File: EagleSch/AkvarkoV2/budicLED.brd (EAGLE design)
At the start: 114.3 x 160 mm, 72 parts, among them IC1 7805T, IC2 4051N, IC3 LF33CV, IC4 ESP01, Q1 BD243C, Q2 BD243C, Q3 BD243C, Q4 BD243C, T1 2N5551, T2 2N5551, T3 2N5551, T4 2N5551, U1 ARDUINOR3-DIMENSION, X1 SMKDSP_1,5/2, X2 SMKDSP_1,5/8, X3 SMKDSP_1,5/3

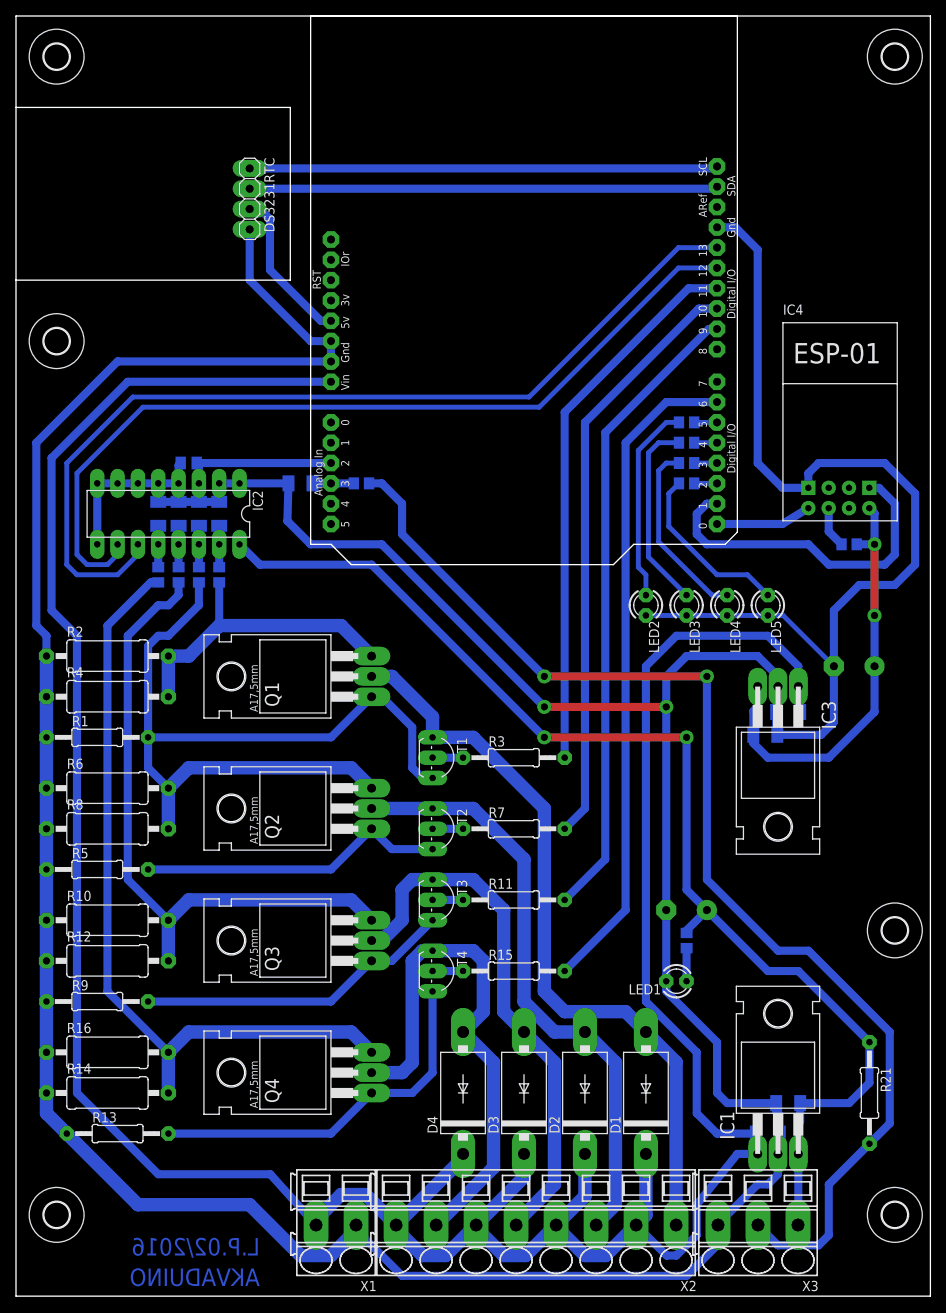
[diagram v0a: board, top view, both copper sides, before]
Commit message: Pridan slot pro SD kartu, odstraneny signalizacni diody.
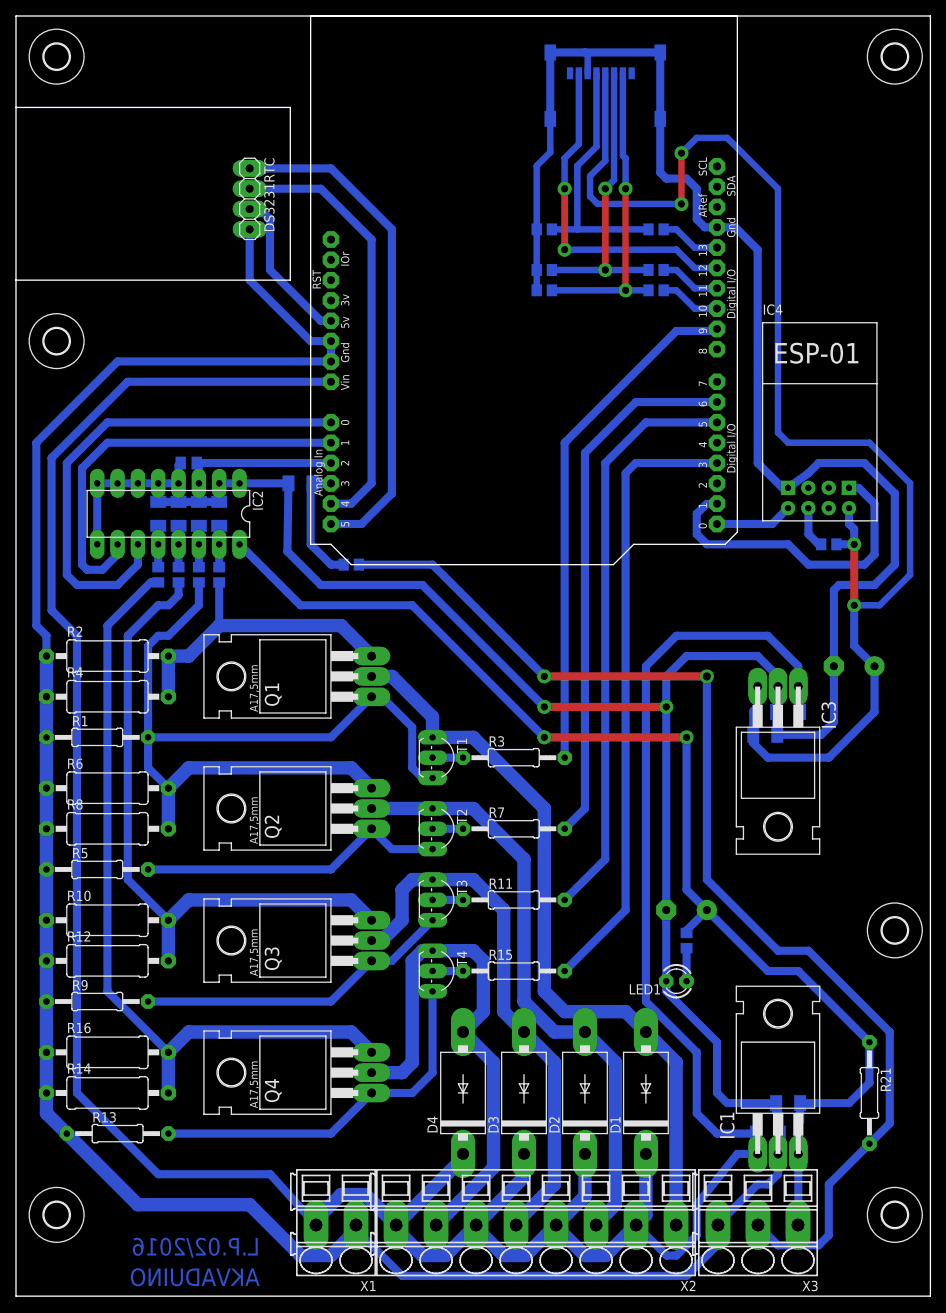
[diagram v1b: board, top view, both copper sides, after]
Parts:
- removed LED2, LED3, LED4, LED5: 2.2V 5mA, led:LED3MM
- added J1: TRANSFLASH-LOCK, sd-mmc:TRANSFLASH-LOCK-SOCK
- added R29: 1k8, rcl:R0805
- added R30: 3k3, rcl:R0805
- R25, R27: value 4k7 -> 1k8
- R26, R28: value 4k7 -> 3k3
- moved R28 32.1 mm to (66.0, 128.3), turned to 0 degrees
- moved R26 32.1 mm to (66.0, 133.3), turned to 0 degrees
- moved R27 24.4 mm to (80.0, 128.3), turned to 0 degrees
- moved R25 24.4 mm to (80.0, 133.3), turned to 0 degrees
- moved R24 10.2 mm to (41.9, 91.4)
- moved IC4 2.54 mm to (100.3, 106.7)
- moved R23 2.54 mm to (101.6, 94.0)
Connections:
- removed net N$20: IC2.11, U1.D13
- removed net N$38: LED5.A, R28.1
- removed net N$39: LED4.A, R27.1
- removed net N$40: LED3.A, R26.1
- removed net N$41: LED2.A, R25.1
- new net MISO: J1.7, U1.D12
- new net MOSI: R27.1, U1.D11
- new net SCK: R25.1, U1.D13
- new net SS: R29.1, U1.D10
- net +3V3: now also J1.4
- net GND: now also J1.6, J1.S1, J1.S2, J1.S3, J1.S4, R26.2, R28.2, R30.2; no longer LED2.K, LED3.K, LED4.K, LED5.K
- net N$13: now also U1.A5; no longer U1.SCL
- net N$15: now also U1.D5; no longer U1.D9
- net N$16: now also R3.2, U1.D9; no longer R28.2, U1.D2
- net N$22: now also U1.D6; no longer U1.D10
- net N$24: now also U1.A4; no longer U1.SDA
- net N$26: now also IC2.11, U1.A0; no longer R27.2, U1.D3
- net N$28: no longer U1.D1
- net N$32: now also J1.5, R25.2, R26.1; no longer IC2.10, U1.D12
- net N$34: now also IC2.10, U1.A1; no longer R3.2, U1.D11
- net N$35: now also U1.D3; no longer U1.D6
- net N$36: now also J1.3, R27.2, R28.1; no longer R26.2, U1.D4
- net N$37: now also J1.2, R29.2, R30.1; no longer R25.2, U1.D5
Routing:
- net +3V3: track 53.5 -> 174.0 mm, vias 2 -> 4
- net N$20: track 116.9 -> 0.00 mm
- net N$32: track 108.2 -> 32.6 mm
- net N$16: track 2.86 -> 64.3 mm
- net N$26: track 2.86 -> 62.1 mm
- net GND: track 582.9 -> 628.3 mm
- net MISO: track 0.00 -> 42.8 mm, vias 0 -> 2
- net N$37: track 2.86 -> 39.3 mm, vias 0 -> 2
- net N$36: track 2.86 -> 37.1 mm, vias 0 -> 2
- net N$41: track 25.0 -> 0.00 mm
- net N$40: track 24.1 -> 0.00 mm
- net N$39: track 23.2 -> 0.00 mm
- net N$38: track 21.9 -> 0.00 mm
- net N$34: track 68.6 -> 51.3 mm
- net N$21: track 5.17 -> 15.2 mm
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
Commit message: Na DPS: - upraveno napajeni - zmenena pouzdra rezistoru u SD karty - seriova linka vyvedena na kolikovou listu - zvetsena sirka spoje GND, doplnen jeden filtracni kapacitor k SD slotu
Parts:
- added C13: 100n, rcl:C1206K
- added JP1: (no value), pinhead:2X04
- added R31: 1k8, rcl:0207/12
- added R32: 3k3, rcl:0207/12
- R25, R26, R27, R28, R29, R30: device rcl:R0805 -> rcl:0207/12
- moved R23 22.9 mm to (101.6, 116.8)
- moved IC4 21.6 mm to (100.3, 128.3)
- moved R21 13.3 mm to (102.9, 12.7)
- moved IC3 12.6 mm to (104.1, 72.4), turned to 270 degrees
- moved C10 11.6 mm to (102.9, 90.2), turned to 180 degrees
- moved R29 8.98 mm to (71.1, 124.5), turned to 90 degrees
- moved R26 8.13 mm to (59.7, 128.3)
- moved R25 8.03 mm to (72.4, 135.9)
- moved R30 7.73 mm to (64.8, 133.3)
- moved J1 7.73 mm to (66.0, 153.7)
- moved R27 6.48 mm to (73.7, 127.0), turned to 90 degrees
- moved R28 4.58 mm to (62.2, 130.8)
- moved C8 3.86 mm to (97.5, 70.8), turned to 90 degrees
- moved C9 2.01 mm to (94.6, 73.7), turned to 270 degrees
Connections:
- new net N$20: IC4.TX, JP1.2, JP1.8
- new net N$38: JP1.5, U1.D1
- new net N$39: IC4.RX, R31.2, R32.1
- new net N$41: JP1.7, U1.D0
- new net N$42: JP1.1, U1.D8
- net +3V3: now also C13.1
- net GND: now also C13.2, R32.2
- net N$25: now also JP1.4, JP1.6, R31.1; no longer IC4.TX, U1.D0
- net N$28: now also JP1.3, U1.D7; no longer IC4.RX
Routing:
- net N$20: track 0.00 -> 32.6 mm
- net N$28: track 39.0 -> 17.6 mm
- net N$39: track 0.00 -> 19.4 mm
- net GND: track 628.3 -> 647.2 mm
- net N$42: track 0.00 -> 16.9 mm
- net N$37: track 39.3 -> 24.5 mm, vias 2 -> 0
- net +3V3: track 174.0 -> 161.7 mm
- net SS: track 7.62 -> 18.7 mm
- net MISO: track 42.8 -> 53.3 mm, vias 2 -> 0
- net MOSI: track 7.62 -> 16.2 mm
- net N$41: track 0.00 -> 6.35 mm
- net N$38: track 0.00 -> 6.35 mm
- net N$32: track 32.6 -> 26.3 mm
- net N$25: track 9.70 -> 6.35 mm
- net SCK: track 7.62 -> 10.9 mm
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
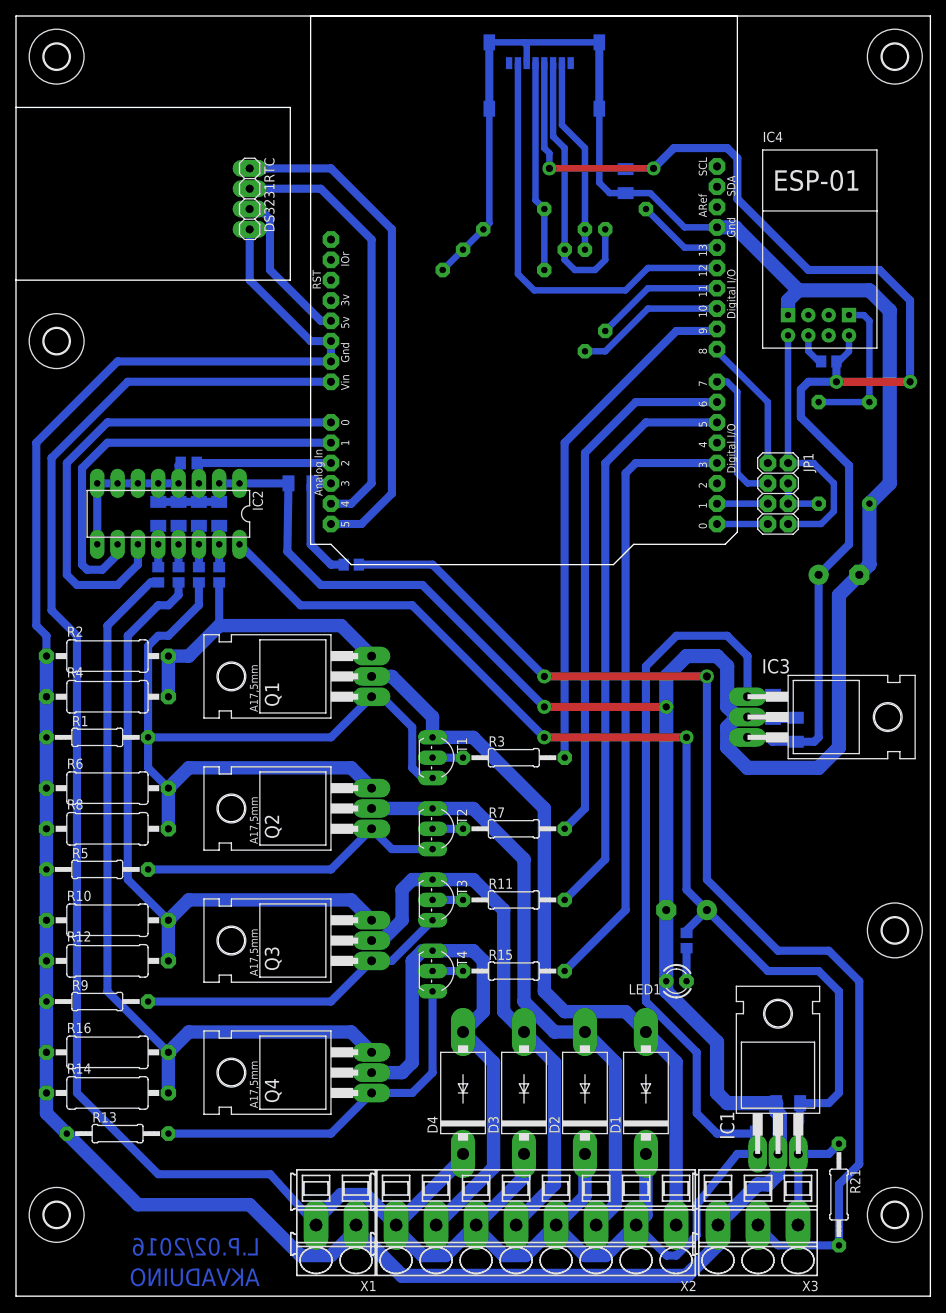
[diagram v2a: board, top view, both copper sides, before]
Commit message: DPS pred vyrobou, nutna kontrola rozmeru.
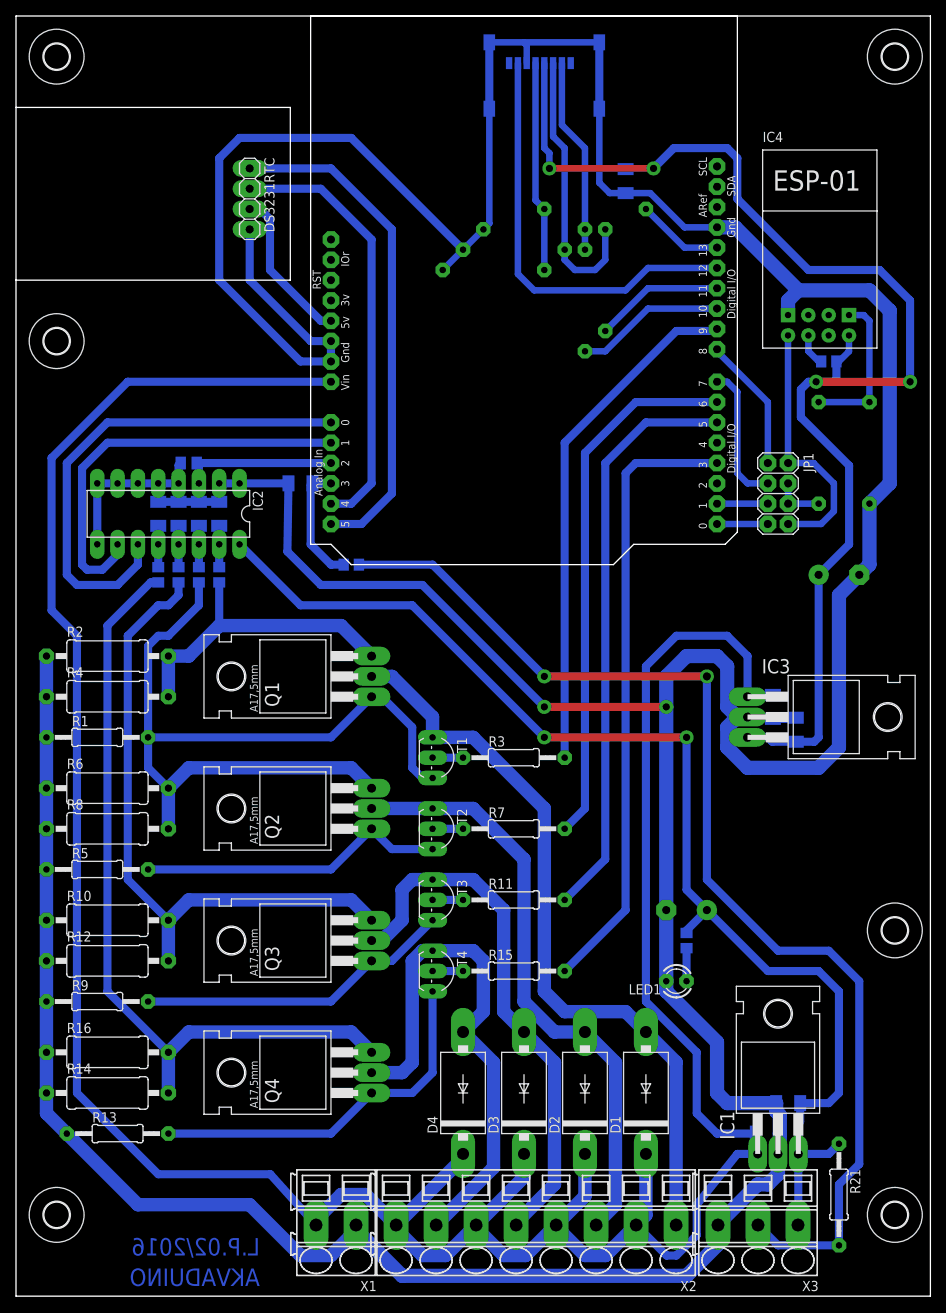
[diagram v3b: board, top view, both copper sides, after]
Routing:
- net +3V3: track 161.7 -> 164.2 mm
- net GND: track 647.2 -> 649.7 mm
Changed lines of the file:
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@@
 <wire x1="34.29" y1="148.59" x2="34.29" y2="127" width="0" layer="20"/>
 <wire x1="34.29" y1="127" x2="0" y2="127" width="0" layer="20"/>
+<dimension x1="0" y1="0" x2="114.3" y2="0" x3="57.15" y3="-8.89" textsize="1.778" layer="48"/>
+<dimension x1="114.3" y1="0" x2="114.3" y2="160.02" x3="124.46" y3="80.01" textsize="1.778" layer="48"/>
+<dimension x1="0" y1="148.59" x2="34.29" y2="148.59" x3="17.145" y3="149.86" textsize="1.778" layer="48"/>
+<dimension x1="0" y1="127" x2="0" y2="148.59" x3="15.24" y3="137.795" textsize="1.778" layer="48"/>
 </plain>
 <attributes>
@@
 <contactref element="U1" pad="GND1"/>
 <wire x1="39.37" y1="116.84" x2="39.37" y2="119.38" width="1.016" layer="16"/>
-<wire x1="12.7" y1="116.84" x2="2.54" y2="106.68" width="1.016" layer="16"/>
 <wire x1="87.75" y1="9.01" x2="92.71" y2="13.97" width="1.778" layer="16"/>
 <wire x1="92.71" y1="13.97" x2="93.98" y2="13.97" width="1.778" layer="16"/>
@@
 <wire x1="42.505" y1="8.295" x2="42.505" y2="8.215" width="1.6764" layer="16"/>
 <wire x1="42.505" y1="8.215" x2="39.37" y2="5.08" width="1.6764" layer="16"/>
-<wire x1="3.81" y1="80.01" x2="3.81" y2="82.55" width="1.016" layer="16"/>
-<wire x1="3.81" y1="82.55" x2="2.54" y2="83.82" width="1.016" layer="16"/>
-<wire x1="2.54" y1="83.82" x2="2.54" y2="106.68" width="1.016" layer="16"/>
-<wire x1="12.7" y1="116.84" x2="39.37" y2="116.84" width="1.016" layer="16"/>
 <wire x1="39.37" y1="119.38" x2="36.83" y2="119.38" width="1.016" layer="16"/>
 <wire x1="36.83" y1="119.38" x2="29.21" y2="127" width="1.016" layer="16"/>
@@
 <wire x1="83.566" y1="133.604" x2="79.2875" y2="137.8825" width="0.8128" layer="16"/>
 <wire x1="76.2" y1="137.8825" x2="79.2875" y2="137.8825" width="0.8128" layer="16"/>
+<wire x1="39.37" y1="116.84" x2="35.56" y2="116.84" width="1.016" layer="16"/>
+<wire x1="35.56" y1="116.84" x2="25.4" y2="127" width="1.016" layer="16"/>
+<wire x1="25.4" y1="127" x2="25.4" y2="142.24" width="1.016" layer="16"/>
+<wire x1="25.4" y1="142.24" x2="27.94" y2="144.78" width="1.016" layer="16"/>
+<wire x1="27.94" y1="144.78" x2="41.91" y2="144.78" width="1.016" layer="16"/>
+<wire x1="41.91" y1="144.78" x2="55.88" y2="130.81" width="1.016" layer="16"/>
 </signal>
 <signal name="N$6">
@@
 <wire x1="98.1075" y1="109.855" x2="98.1075" y2="113.3475" width="1.016" layer="16"/>
 <wire x1="98.1075" y1="113.3475" x2="99.06" y2="114.3" width="1.016" layer="16"/>
-<wire x1="102.5525" y1="114.3" x2="99.06" y2="114.3" width="1.016" layer="16"/>
-<via x="102.5525" y="114.3" extent="1-16" drill="0.9" diameter="1.778"/>
-<wire x1="102.5525" y1="114.3" x2="111.76" y2="114.3" width="1.016" layer="1"/>
+<wire x1="100.0125" y1="114.3" x2="99.06" y2="114.3" width="1.016" layer="16"/>
+<via x="100.0125" y="114.3" extent="1-16" drill="0.9" diameter="1.778"/>
+<wire x1="100.0125" y1="114.3" x2="111.76" y2="114.3" width="1.016" layer="1"/>
 <via x="111.76" y="114.3" extent="1-16" drill="0.9" diameter="1.778"/>
 <wire x1="111.76" y1="114.3" x2="111.76" y2="124.46" width="1.016" layer="16"/>
@@
 <wire x1="90.17" y1="137.16" x2="90.17" y2="142.24" width="1.016" layer="16"/>
 <wire x1="102.55" y1="116.84" x2="102.55" y2="114.3025" width="1.016" layer="16"/>
-<wire x1="102.55" y1="114.3025" x2="102.5525" y2="114.3" width="1.016" layer="16"/>
+<wire x1="102.55" y1="114.3025" x2="100.0125" y2="114.3" width="1.016" layer="16"/>
 <wire x1="90.17" y1="142.24" x2="88.9" y2="143.51" width="1.016" layer="16"/>
 <wire x1="88.9" y1="143.51" x2="82.2325" y2="143.51" width="1.016" layer="16"/>
